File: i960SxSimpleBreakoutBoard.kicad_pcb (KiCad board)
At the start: 4 copper layers, 98.6 x 85.3 mm, 32 parts, among them J1 Conn_01x23, J2 Address Lines Lower, J3 Data Lines, J4 Address Lines Upper, U1 74HC573, U2 74HC573, U3 80960Sx, U4 74HC245, U5 74HC245

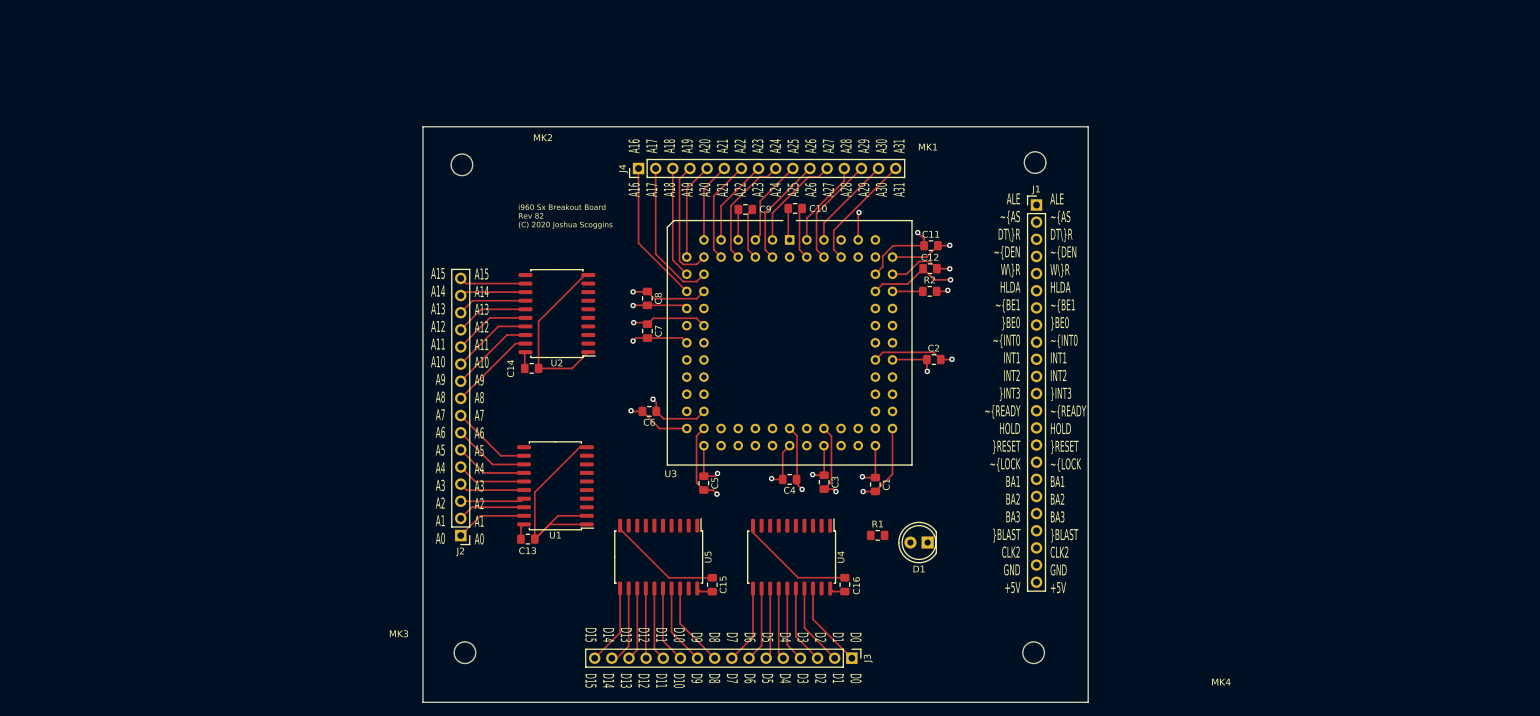
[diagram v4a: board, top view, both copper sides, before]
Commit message: Breakout getting more complex, need to switch to 40 pin cables
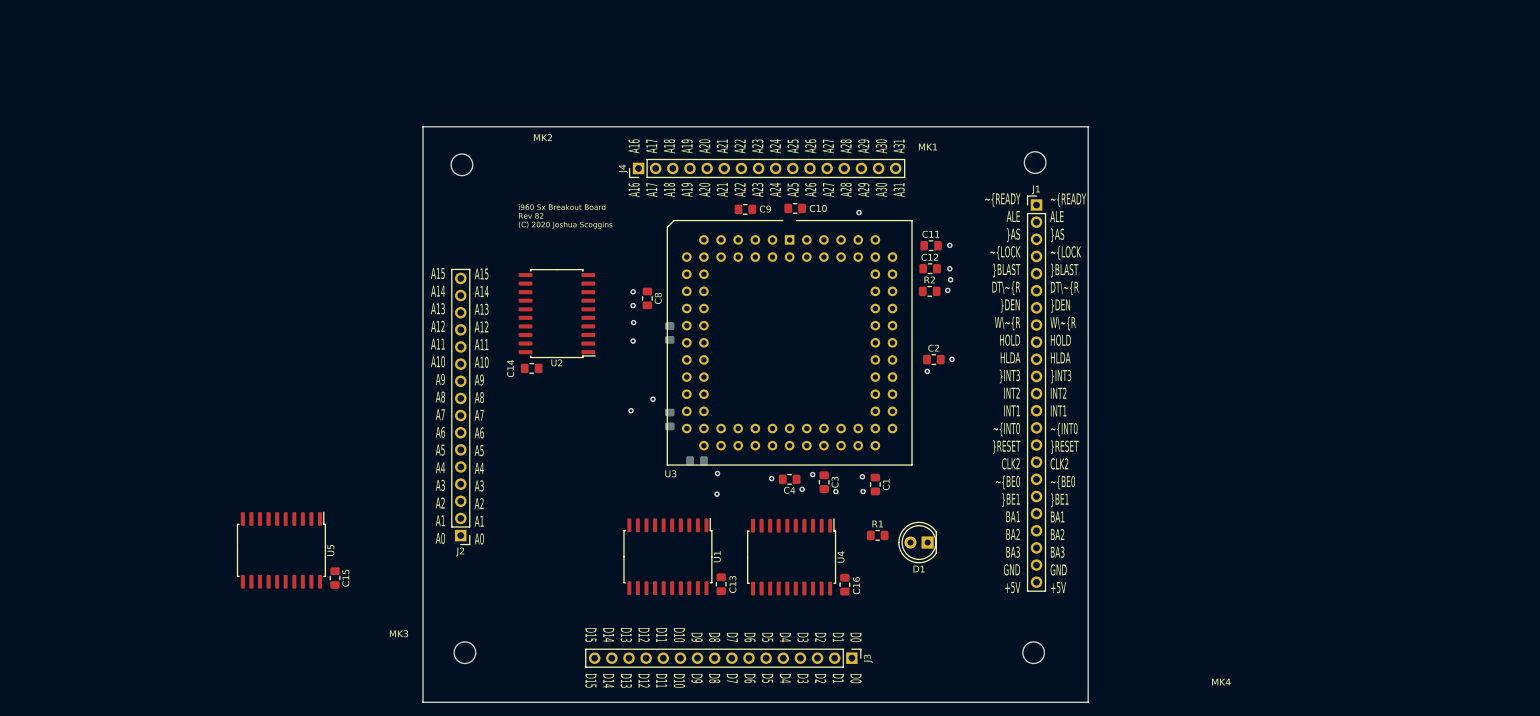
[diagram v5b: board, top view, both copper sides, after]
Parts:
- C5, C6, C7: moved to B.Cu
- moved U5 55.9 mm to (-74.3, 43.8)
- moved C15 55.9 mm to (-66.3, 47.9)
- moved C13 29.4 mm to (-9.10, 48.9), turned to 90 degrees
- moved U1 19.7 mm to (-17.0, 44.8), turned to 270 degrees
- moved C5 3.44 mm to (-12.7, 30.6), turned to 180 degrees
- moved C7 3.31 mm to (-16.7, 11.6)
- moved C6 3.26 mm to (-16.7, 24.4), turned to 270 degrees
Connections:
- J1 pad 1: /ALE -> /~READY
- J1 pad 10: /INT1 -> /HLDA
- J1 pad 11: /INT2 -> /~INT3
- J1 pad 12: /~INT3 -> /INT2
- J1 pad 13: /~READY -> /INT1
- J1 pad 14: /HOLD -> /~INT0
- J1 pad 16: /~LOCK -> /CLK2
- J1 pad 17: /BA1 -> /~BE0
- J1 pad 18: /BA2 -> /~BE1
- J1 pad 19: /BA3 -> /BA1
- J1 pad 2: /~AS -> /ALE
- J1 pad 20: /~BLAST -> /BA2
- J1 pad 21: /CLK2 -> /BA3
- J1 pad 3: /DT\~R -> /~AS
- J1 pad 4: /~DEN -> /~LOCK
- J1 pad 5: /W\~R -> /~BLAST
- J1 pad 6: /HLDA -> /DT\~R
- J1 pad 7: /~BE1 -> /~DEN
- J1 pad 8: /~BE0 -> /W\~R
- J1 pad 9: /~INT0 -> /HOLD
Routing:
- net GND: track 212.1 -> 0.00 mm
- net +5V: track 118.3 -> 0.00 mm, vias 11 -> 10
- net /A17: track 22.0 -> 0.00 mm
- net /A16: track 21.2 -> 0.00 mm
- net /A19: track 18.6 -> 0.00 mm
- net /A31: track 17.4 -> 0.00 mm
- net /A24: track 17.0 -> 0.00 mm
- net /A18: track 16.5 -> 0.00 mm
- net /A29: track 16.3 -> 0.00 mm
- net /A26: track 16.3 -> 0.00 mm
- net /A22: track 15.3 -> 0.00 mm
- net /A27: track 14.8 -> 0.00 mm
- net /A20: track 14.4 -> 0.00 mm
- net /A30: track 13.9 -> 0.00 mm
- net /A8: track 13.0 -> 0.00 mm
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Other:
- board text added: "~READY ALE ~AS ~LOCK ~BLAST DT\~R ~DEN W\~R HOLD HLDA ~INT3 INT2 INT1 ~INT0 ~RESET CLK2 ~BE0 ~BE1 BA1 BA2 BA3 GND +5V"
- board text removed: "ALE ~AS DT\~R ~DEN W\~R HLDA ~BE1 ~BE0 ~INT0 INT1 INT2 ~INT3 ~READY HOLD ~RESET ~LOCK BA1 BA2 BA3 ~BLAST CLK2 GND +5V"

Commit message: Layout complete, no rpi cable at this time
Too many lines, to put through a single cable
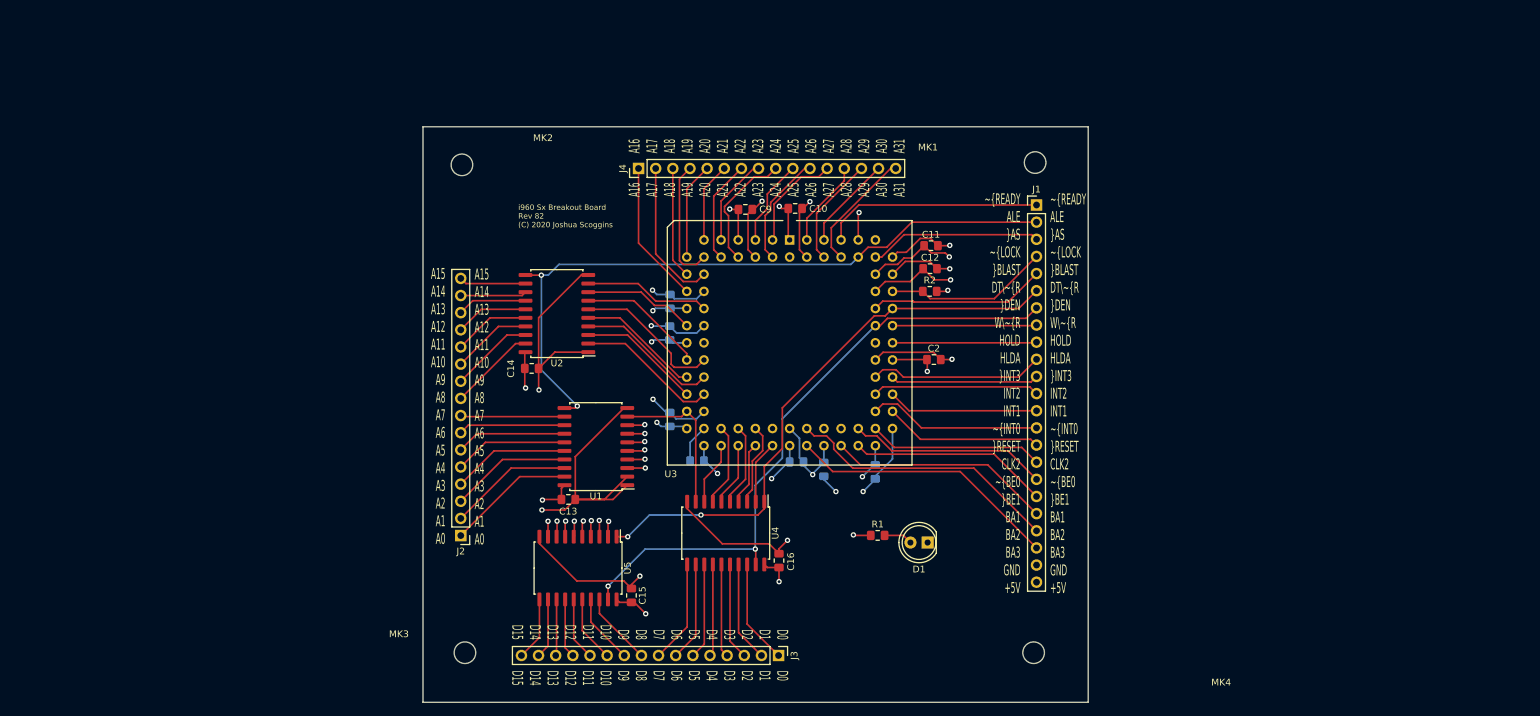
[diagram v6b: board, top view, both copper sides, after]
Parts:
- C1, C3, C4, C8: moved to B.Cu
- moved U5 44.0 mm to (-30.3, 46.5)
- moved C15 44.0 mm to (-22.4, 50.5)
- moved C13 25.9 mm to (-31.7, 36.3), turned to 0 degrees
- moved U1 19.5 mm to (-27.7, 28.5), turned to 180 degrees
- moved J3 10.9 mm to (-0.60, 59.4)
- moved U4 10.4 mm to (-8.43, 41.3)
- moved C16 10.4 mm to (-0.54, 45.4)
- moved C8 3.38 mm to (-16.7, 6.95)
- moved C4 2.79 mm to (2.07, 30.7)
- moved C3 1.90 mm to (6.10, 31.8)
- moved C1 1.87 mm to (13.7, 32.2)
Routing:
- net GND: track 0.00 -> 201.9 mm, vias 11 -> 16
- net +5V: track 0.00 -> 124.2 mm, vias 10 -> 17
- net /ALE: track 0.00 -> 102.6 mm, vias 0 -> 2
- net /~DEN: track 0.00 -> 93.8 mm, vias 0 -> 2
- net /DT\~R: track 0.00 -> 84.5 mm, vias 0 -> 2
- net /AD15: track 0.00 -> 63.6 mm, vias 0 -> 1
- net /AD12: track 0.00 -> 61.1 mm, vias 0 -> 1
- net /AD10: track 0.00 -> 57.6 mm, vias 0 -> 1
- net /AD14: track 0.00 -> 57.1 mm, vias 0 -> 1
- net /AD13: track 0.00 -> 56.2 mm, vias 0 -> 1
- net /AD8: track 0.00 -> 53.1 mm, vias 0 -> 1
- net /AD11: track 0.00 -> 52.7 mm, vias 0 -> 1
- net /AD9: track 0.00 -> 49.4 mm, vias 0 -> 1
- net /BA2: track 0.00 -> 40.8 mm
- net /BA3: track 0.00 -> 40.3 mm
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
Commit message: Get rid of the mounting holes and put multiplexed lines on a single edge
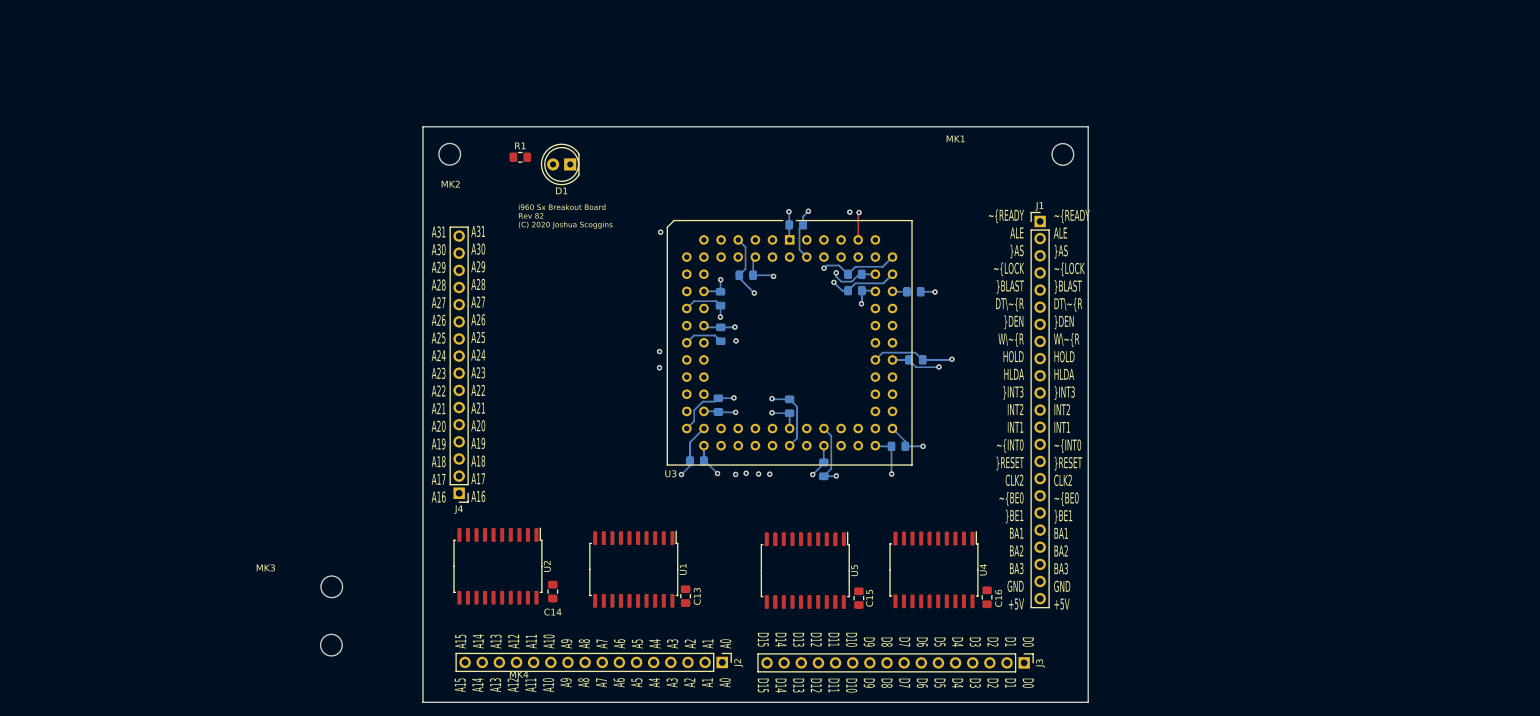
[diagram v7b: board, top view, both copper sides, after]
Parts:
- C10, C11, C12, C2, C9, R2: moved to B.Cu
- moved MK4 104.0 mm to (-66.9, 57.9)
- moved D1 77.1 mm to (-31.5, -13.3)
- moved R1 77.1 mm to (-38.9, -14.4)
- moved J4 55.0 mm to (-47.9, 35.4), turned to 180 degrees
- moved J2 43.1 mm to (-8.95, 60.4), turned to 270 degrees
- moved U2 38.5 mm to (-42.2, 46.2), turned to 270 degrees
- moved J3 36.4 mm to (35.8, 60.5)
- moved C15 33.7 mm to (11.3, 50.9)
- moved U5 33.7 mm to (3.36, 46.8)
- moved C14 33.2 mm to (-34.1, 49.9), turned to 90 degrees
- moved U4 31.3 mm to (22.4, 46.7)
- moved C16 31.3 mm to (30.3, 50.8)
- moved C13 22.5 mm to (-14.4, 50.6), turned to 90 degrees
- moved MK3 22.0 mm to (-66.8, 49.2)
- moved U1 19.0 mm to (-22.1, 46.7), turned to 270 degrees
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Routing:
- net /ALE: track 102.6 -> 0.00 mm, vias 2 -> 0
- net /~DEN: track 93.8 -> 0.00 mm, vias 2 -> 0
- net /DT\~R: track 84.5 -> 0.00 mm, vias 2 -> 0
- net /AD15: track 63.6 -> 0.00 mm, vias 1 -> 0
- net /AD12: track 61.1 -> 0.00 mm, vias 1 -> 0
- net /AD10: track 57.6 -> 0.00 mm, vias 1 -> 0
- net /AD14: track 57.1 -> 0.00 mm, vias 1 -> 0
- net /AD13: track 56.2 -> 0.00 mm, vias 1 -> 0
- net /AD8: track 53.1 -> 0.00 mm, vias 1 -> 0
- net /AD11: track 52.7 -> 0.00 mm, vias 1 -> 0
- net /AD9: track 49.4 -> 0.00 mm, vias 1 -> 0
- net /BA2: track 40.8 -> 0.00 mm
- net /BA3: track 40.3 -> 0.00 mm
- net GND: track 201.9 -> 164.1 mm
- net /AD1: track 34.6 -> 0.00 mm, vias 1 -> 0
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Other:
- board text added: "A31 A30 A29 A28 A27 A26 A25 A24 A23 A22 A21 A20 A19 A18 A17 A16"
- board text removed: "A16 A17 A18 A19 A20 A21 A22 A23 A24 A25 A26 A27 A28 A29 A30 A31"

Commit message: Address lines grouped together again
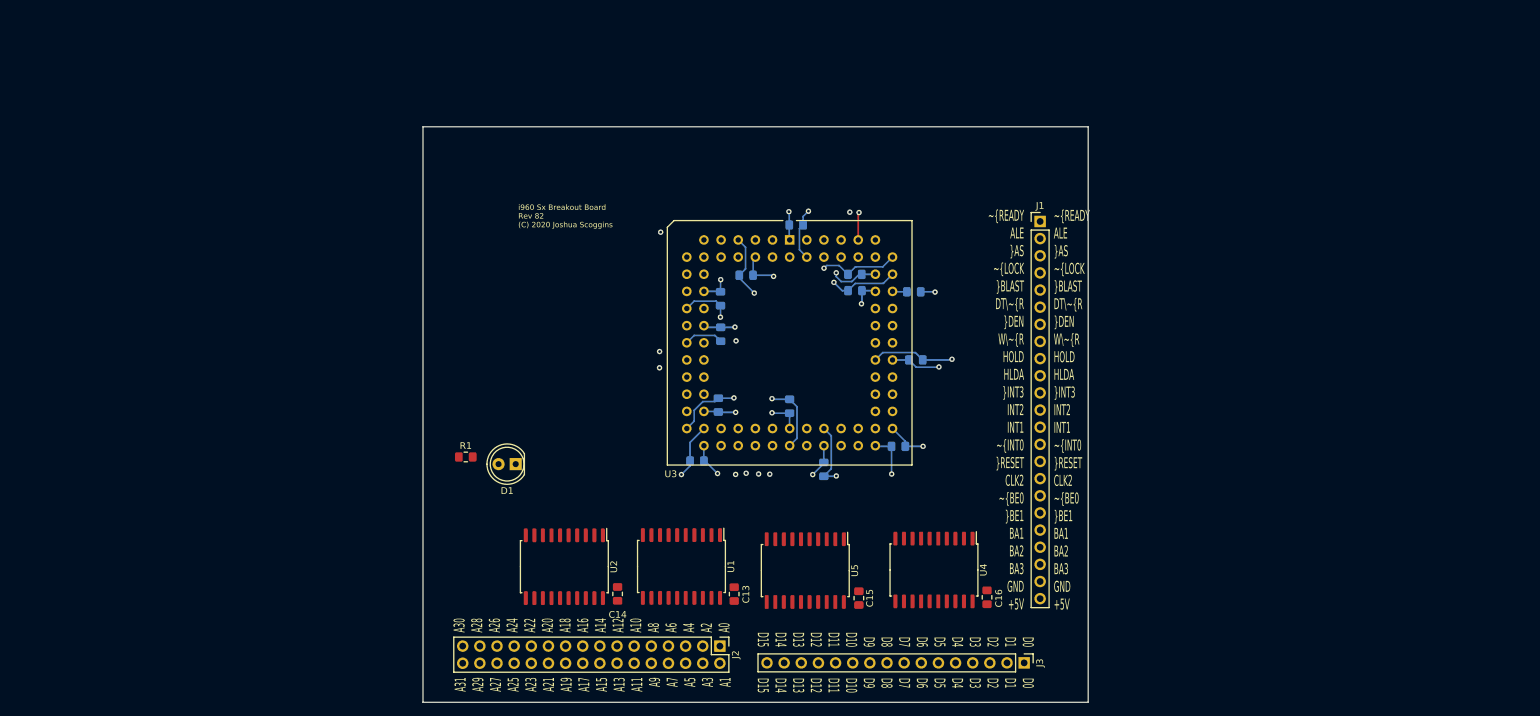
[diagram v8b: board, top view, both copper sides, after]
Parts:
- removed J4: Address Lines Upper, Connector_PinHeader_2.54mm:PinHeader_1x16_P2.54mm_Vertical
- removed MK1, MK2, MK3, MK4: Mounting_Hole, MountingHole:MountingHole_3.2mm_M3
- J2: value Address Lines Lower -> Conn_02x16_Counter_Clockwise; footprint Connector_PinHeader_2.54mm:PinHeader_1x16_P2.54mm_Vertical -> Connector_PinHeader_2.54mm:PinHeader_2x16_P2.54mm_Vertical
- moved D1 45.1 mm to (-39.5, 31.1)
- moved R1 45.1 mm to (-46.9, 30.0)
- moved U2 9.84 mm to (-32.3, 46.3)
- moved C14 9.61 mm to (-24.5, 50.3)
- moved C13 7.20 mm to (-7.18, 50.3)
- moved U1 7.08 mm to (-15.0, 46.2)
- moved J2 2.44 mm to (-9.30, 58.0)
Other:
- board text added: "A30 A28 A26 A24 A22 A20 A18 A16 A14 A12 A10 A8 A6 A4 A2 A0"
- board text added: "A31 A29 A27 A25 A23 A21 A19 A17 A15 A13 A11 A9 A7 A5 A3 A1"
- board text removed: "A15 A14 A13 A12 A11 A10 A9 A8 A7 A6 A5 A4 A3 A2 A1 A0"
- board text removed: "A31 A30 A29 A28 A27 A26 A25 A24 A23 A22 A21 A20 A19 A18 A17 A16"
